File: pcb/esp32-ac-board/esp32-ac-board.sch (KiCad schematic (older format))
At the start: 5 parts, among them Q1 Q_NPN_BCE

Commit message: Fix schematic, redo PCB
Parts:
- added J1, J2: Conn_01x15, Connector_PinHeader_2.54mm:PinHeader_1x15_P2.54mm_Vertical, symbol Connector_Generic:Conn_01x15
- added SW1: SW_Push, Button_Switch_THT:SW_PUSH-12mm, symbol Switch:SW_Push
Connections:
- net labels added: 1, 13, 15, 16, 17, 18, 19, 2, 21, 22, 23, 25, 27, 3, 32, 33, 34, 35, 36, 39, 4, 5, BTN, EN, SEND, TEMP, VCC
- net labels removed: VIN
- wire segments 42 -> 54
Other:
- moved on the sheet: DHT_22, R1

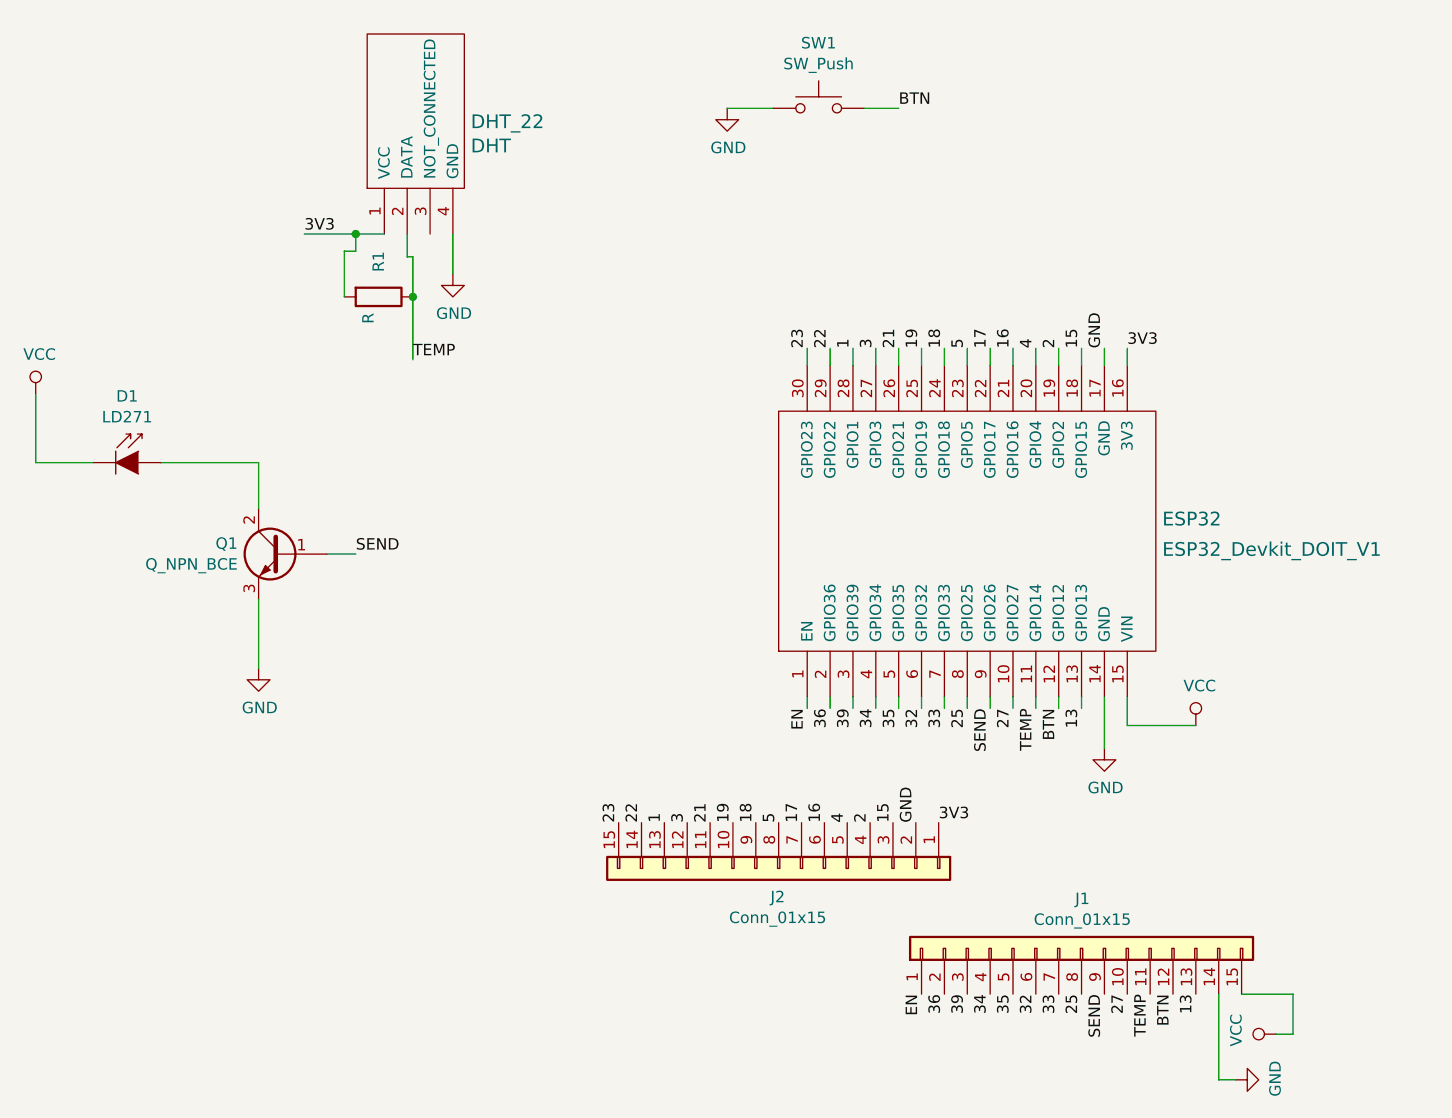
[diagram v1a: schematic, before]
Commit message: Use 5V signal like in https://hackaday.com/2016/11/17/creating-a-pcb-in-everything-kicad-part-1/
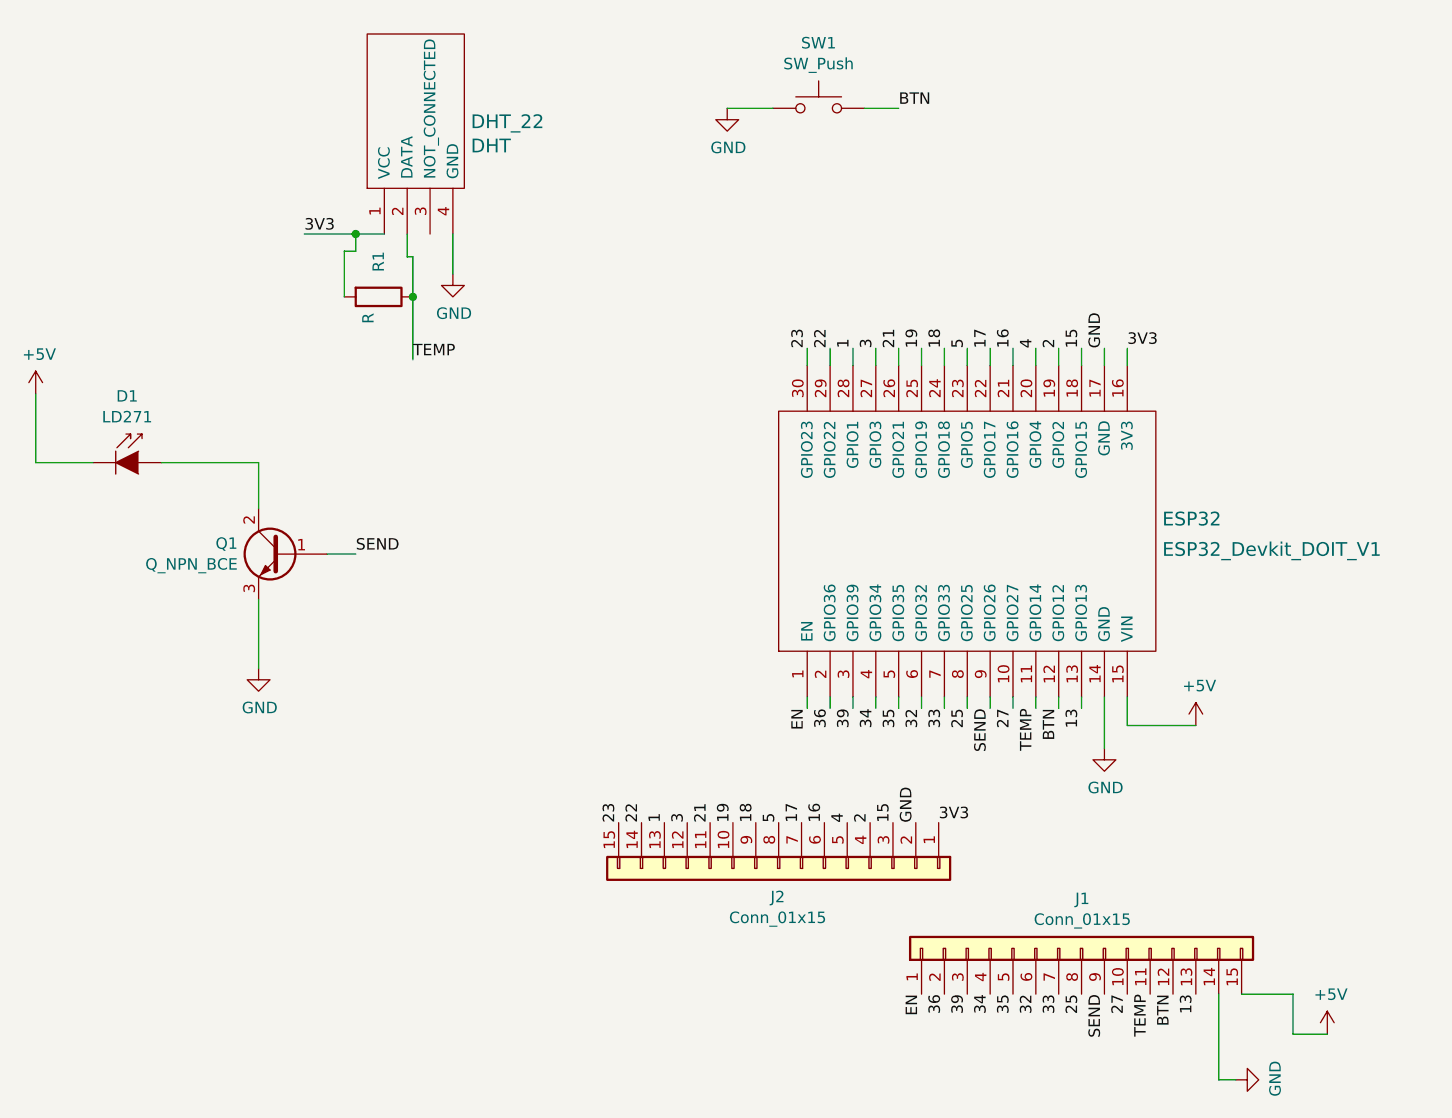
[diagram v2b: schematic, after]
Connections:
- net VCC renamed +5V
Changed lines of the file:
@@
 Wire Wire Line
 	7075 2850 7075 2675
-$Comp
-L power:VCC #PWR01
-U 1 1 5CFF060E
-P 5250 3375
-F 0 "#PWR01" H 5250 3225 50  0001 C CNN
-F 1 "VCC" H 5267 3548 50  0000 C CNN
-F 2 "" H 5250 3375 50  0001 C CNN
-F 3 "" H 5250 3375 50  0001 C CNN
-	1    5250 3375
-	1    0    0    -1
-$EndComp
 Wire Wire Line
 	5250 3675 5500 3675
 Wire Wire Line
 	5250 3375 5250 3675
-$Comp
-L power:VCC #PWR05
-U 1 1 5CFF29F8
-P 10325 4825
-F 0 "#PWR05" H 10325 4675 50  0001 C CNN
-F 1 "VCC" H 10342 4998 50  0000 C CNN
-F 2 "" H 10325 4825 50  0001 C CNN
-F 3 "" H 10325 4825 50  0001 C CNN
-	1    10325 4825
-	1    0    0    -1
-$EndComp
 Wire Wire Line
 	10325 4825 10025 4825
@@
 Wire Wire Line
 	10500 6375 10425 6375
-$Comp
-L power:VCC #PWR0103
-U 1 1 5D01AC3E
-P 10675 6175
-F 0 "#PWR0103" H 10675 6025 50  0001 C CNN
-F 1 "VCC" H 10692 6348 50  0000 C CNN
-F 2 "" H 10675 6175 50  0001 C CNN
-F 3 "" H 10675 6175 50  0001 C CNN
-	1    10675 6175
-	0    -1   -1   0
-$EndComp
-Wire Wire Line
-	10675 6175 10750 6175
+Wire Wire Line
+	10900 6175 10750 6175
 Wire Wire Line
 	10750 6175 10750 6000
@@
 Wire Wire Line
 	8875 2125 9025 2125
+$Comp
+L power:+5V #PWR?
+U 1 1 5CFF5954
+P 5250 3375
+F 0 "#PWR?" H 5250 3225 50  0001 C CNN
+F 1 "+5V" H 5265 3548 50  0000 C CNN
+F 2 "" H 5250 3375 50  0001 C CNN
+F 3 "" H 5250 3375 50  0001 C CNN
+	1    5250 3375
+	1    0    0    -1
+$EndComp
+$Comp
+L power:+5V #PWR?
+U 1 1 5CFF6215
+P 10325 4825
+F 0 "#PWR?" H 10325 4675 50  0001 C CNN
+F 1 "+5V" H 10340 4998 50  0000 C CNN
+F 2 "" H 10325 4825 50  0001 C CNN
+F 3 "" H 10325 4825 50  0001 C CNN
+	1    10325 4825
+	1    0    0    -1
+$EndComp
+$Comp
+L power:+5V #PWR?
+U 1 1 5CFF718F
+P 10900 6175
+F 0 "#PWR?" H 10900 6025 50  0001 C CNN
+F 1 "+5V" H 10915 6348 50  0000 C CNN
+F 2 "" H 10900 6175 50  0001 C CNN
+F 3 "" H 10900 6175 50  0001 C CNN
+	1    10900 6175
+	1    0    0    -1
+$EndComp
 $EndSCHEMATC

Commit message: Add traces
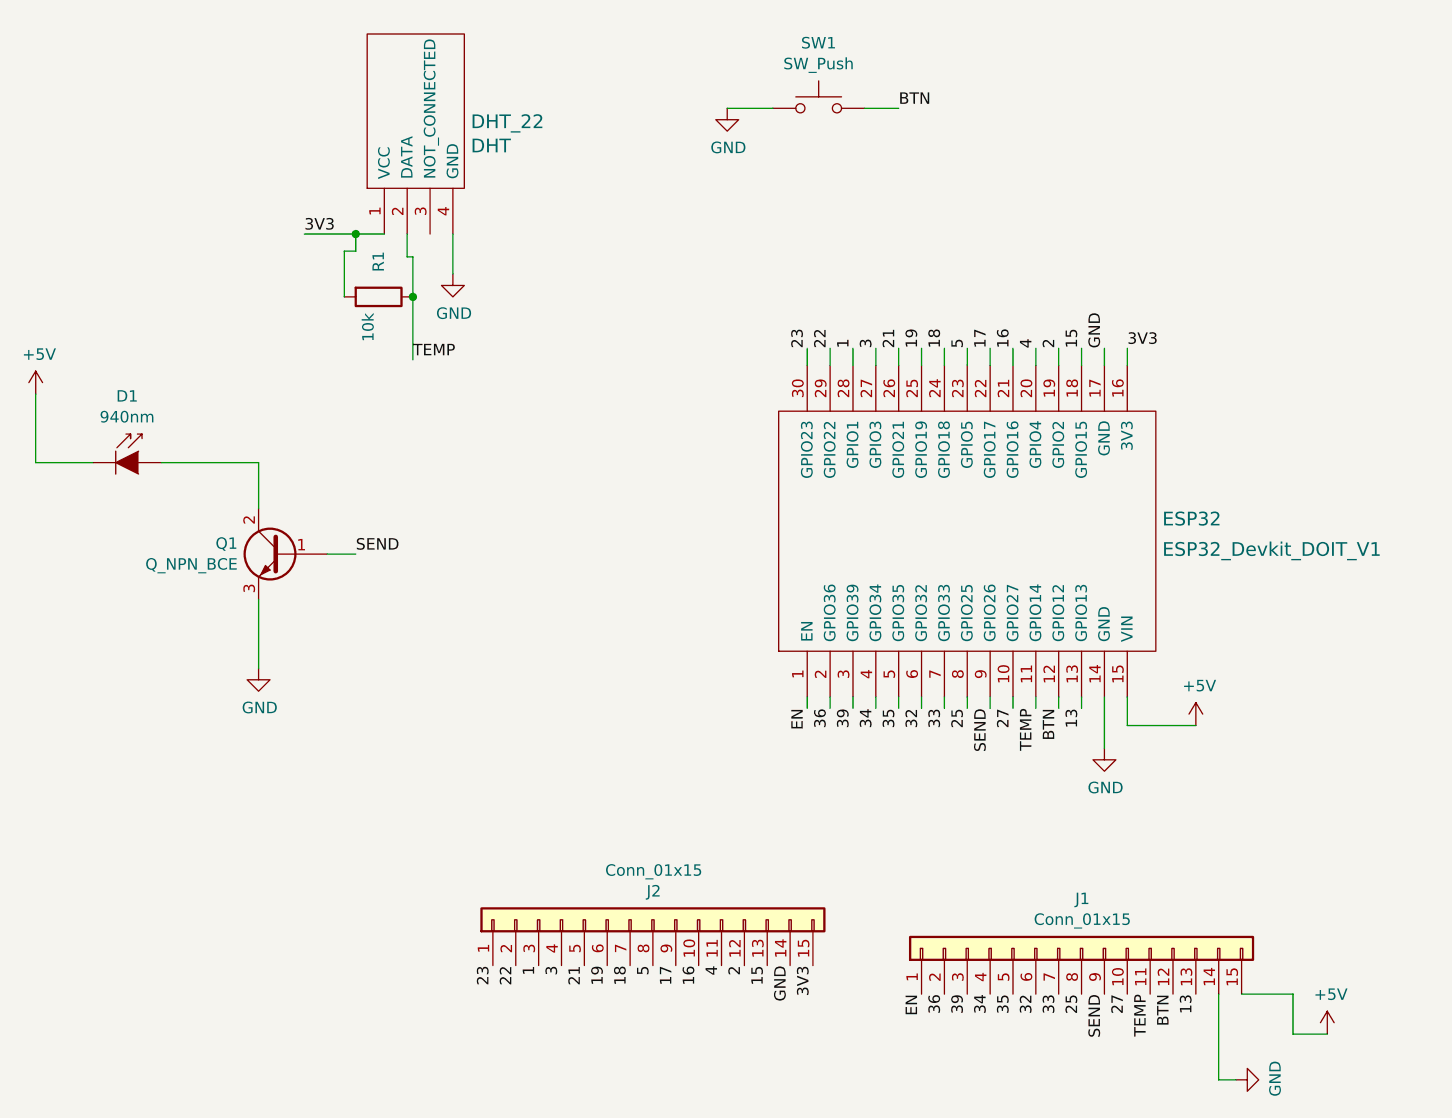
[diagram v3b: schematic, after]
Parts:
- D1: value LD271 -> 940nm
- R1: value R -> 10k
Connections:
- net 1: now also J2.3 (Pin_3); no longer J2.13 (Pin_13)
- net 15: now also J2.13 (Pin_13); no longer J2.3 (Pin_3)
- net 16: now also J2.10 (Pin_10); no longer J2.6 (Pin_6)
- net 17: now also J2.9 (Pin_9); no longer J2.7 (Pin_7)
- net 18: now also J2.7 (Pin_7); no longer J2.9 (Pin_9)
- net 19: now also J2.6 (Pin_6); no longer J2.10 (Pin_10)
- net 2: now also J2.12 (Pin_12); no longer J2.4 (Pin_4)
- net 21: now also J2.5 (Pin_5); no longer J2.11 (Pin_11)
- net 22: now also J2.2 (Pin_2); no longer J2.14 (Pin_14)
- net 23: now also J2.1 (Pin_1); no longer J2.15 (Pin_15)
- net 3: now also J2.4 (Pin_4); no longer J2.12 (Pin_12)
- net 3V3: now also J2.15 (Pin_15); no longer J2.1 (Pin_1)
- net 4: now also J2.11 (Pin_11); no longer J2.5 (Pin_5)
- net GND: now also J2.14 (Pin_14); no longer J2.2 (Pin_2)
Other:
- moved on the sheet: J2
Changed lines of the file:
@@
 P 5700 3675
 F 0 "D1" H 5650 3965 50  0000 C CNN
-F 1 "LD271" H 5650 3874 50  0000 C CNN
+F 1 "940nm" H 5650 3874 50  0000 C CNN
 F 2 "LED_THT:LED_D5.0mm_IRGrey" H 5700 3850 50  0001 C CNN
 F 3 "http://www.alliedelec.com/m/d/40788c34903a719969df15f1fbea1056.pdf" H 5650 3675 50  0001 C CNN
@@
 P 6750 2950
 F 0 "R1" H 6550 2950 50  0000 L CNN
-F 1 "R" H 6820 2905 50  0000 L CNN
+F 1 "10k" H 6820 2905 50  0000 L CNN
 F 2 "Resistor_THT:R_Axial_DIN0204_L3.6mm_D1.6mm_P5.08mm_Horizontal" V 6680 2950 50  0001 C CNN
 F 3 "~" H 6750 2950 50  0001 C CNN
@@
 L Connector_Generic:Conn_01x15 J2
 U 1 1 5D00F2B8
-P 8500 5450
-F 0 "J2" V 8625 5446 50  0000 C CNN
-F 1 "Conn_01x15" V 8716 5446 50  0000 C CNN
-F 2 "Connector_PinHeader_2.54mm:PinHeader_1x15_P2.54mm_Vertical" H 8500 5450 50  0001 C CNN
-F 3 "~" H 8500 5450 50  0001 C CNN
-	1    8500 5450
-	0    1    1    0
+P 7950 5675
+F 0 "J2" V 8075 5671 50  0000 C CNN
+F 1 "Conn_01x15" V 8166 5671 50  0000 C CNN
+F 2 "Connector_PinHeader_2.54mm:PinHeader_1x15_P2.54mm_Vertical" H 7950 5675 50  0001 C CNN
+F 3 "~" H 7950 5675 50  0001 C CNN
+	1    7950 5675
+	0    -1   -1   0
 $EndComp
 Text Label 8625 4750 3    50   ~ 0
@@
 Wire Wire Line
 	6225 4275 6225 4575
-Text Label 9200 5250 0    50   ~ 0
+Text Label 8650 5875 3    50   ~ 0
 3V3
-Text Label 9100 5250 1    50   ~ 0
+Text Label 8550 5875 3    50   ~ 0
 GND
-Text Label 9000 5250 1    50   ~ 0
+Text Label 8450 5875 3    50   ~ 0
 15
-Text Label 8900 5250 1    50   ~ 0
+Text Label 8350 5875 3    50   ~ 0
 2
 Text Label 9925 3175 1    50   ~ 0
@@
 Text Label 8625 3175 1    50   ~ 0
 23
-Text Label 8800 5250 1    50   ~ 0
+Text Label 8250 5875 3    50   ~ 0
 4
-Text Label 8700 5250 1    50   ~ 0
+Text Label 8150 5875 3    50   ~ 0
 16
-Text Label 8600 5250 1    50   ~ 0
+Text Label 8050 5875 3    50   ~ 0
 17
-Text Label 8500 5250 1    50   ~ 0
+Text Label 7950 5875 3    50   ~ 0
 5
-Text Label 8400 5250 1    50   ~ 0
+Text Label 7850 5875 3    50   ~ 0
 18
-Text Label 8300 5250 1    50   ~ 0
+Text Label 7750 5875 3    50   ~ 0
 19
-Text Label 8200 5250 1    50   ~ 0
+Text Label 7650 5875 3    50   ~ 0
 21
-Text Label 8100 5250 1    50   ~ 0
+Text Label 7550 5875 3    50   ~ 0
 3
-Text Label 8000 5250 1    50   ~ 0
+Text Label 7450 5875 3    50   ~ 0
 1
-Text Label 7900 5250 1    50   ~ 0
+Text Label 7350 5875 3    50   ~ 0
 22
-Text Label 7800 5250 1    50   ~ 0
+Text Label 7250 5875 3    50   ~ 0
 23
 $Comp
@@
 	8875 2125 9025 2125
 $Comp
-L power:+5V #PWR?
+L power:+5V #PWR0103
 U 1 1 5CFF5954
 P 5250 3375
-F 0 "#PWR?" H 5250 3225 50  0001 C CNN
+F 0 "#PWR0103" H 5250 3225 50  0001 C CNN
 F 1 "+5V" H 5265 3548 50  0000 C CNN
 F 2 "" H 5250 3375 50  0001 C CNN
@@
 $EndComp
 $Comp
-L power:+5V #PWR?
+L power:+5V #PWR0104
 U 1 1 5CFF6215
 P 10325 4825
-F 0 "#PWR?" H 10325 4675 50  0001 C CNN
+F 0 "#PWR0104" H 10325 4675 50  0001 C CNN
 F 1 "+5V" H 10340 4998 50  0000 C CNN
 F 2 "" H 10325 4825 50  0001 C CNN
@@
 $EndComp
 $Comp
-L power:+5V #PWR?
+L power:+5V #PWR0105
 U 1 1 5CFF718F
 P 10900 6175
-F 0 "#PWR?" H 10900 6025 50  0001 C CNN
+F 0 "#PWR0105" H 10900 6025 50  0001 C CNN
 F 1 "+5V" H 10915 6348 50  0000 C CNN
 F 2 "" H 10900 6175 50  0001 C CNN

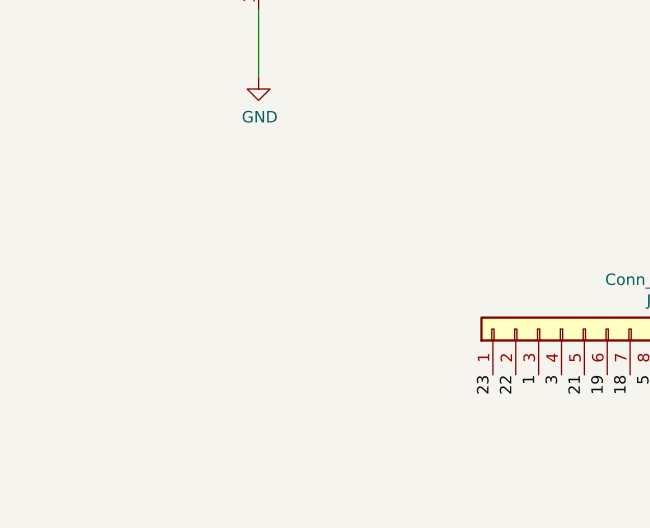
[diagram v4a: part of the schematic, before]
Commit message: add screw terminal for power
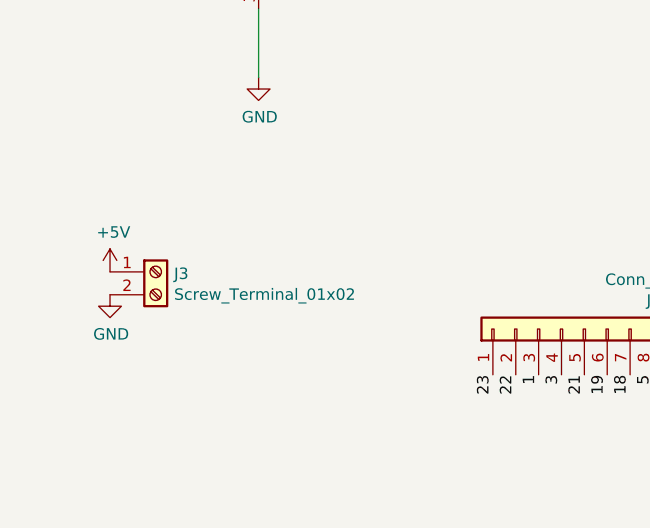
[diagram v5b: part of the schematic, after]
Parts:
- added J3: Screw_Terminal_01x02, TerminalBlock:TerminalBlock_bornier-2_P5.08mm, symbol Connector:Screw_Terminal_01x02
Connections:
- net +5V: now also J3.1 (Pin_1)
- net GND: now also J3.2 (Pin_2)
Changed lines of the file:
@@
 Text Label 9925 3175 1    50   ~ 0
 GND
+$Comp
+L Connector:Screw_Terminal_01x02 J3
+U 1 1 5D014690
+P 5775 5425
+F 0 "J3" H 5855 5417 50  0000 L CNN
+F 1 "Screw_Terminal_01x02" H 5855 5326 50  0000 L CNN
+F 2 "TerminalBlock:TerminalBlock_bornier-2_P5.08mm" H 5775 5425 50  0001 C CNN
+F 3 "~" H 5775 5425 50  0001 C CNN
+	1    5775 5425
+	1    0    0    -1
+$EndComp
+$Comp
+L power:+5V #PWR0106
+U 1 1 5D016026
+P 5575 5425
+F 0 "#PWR0106" H 5575 5275 50  0001 C CNN
+F 1 "+5V" H 5590 5598 50  0000 C CNN
+F 2 "" H 5575 5425 50  0001 C CNN
+F 3 "" H 5575 5425 50  0001 C CNN
+	1    5575 5425
+	1    0    0    -1
+$EndComp
+$Comp
+L power:GND #PWR0107
+U 1 1 5D016A88
+P 5575 5525
+F 0 "#PWR0107" H 5575 5275 50  0001 C CNN
+F 1 "GND" H 5580 5352 50  0000 C CNN
+F 2 "" H 5575 5525 50  0001 C CNN
+F 3 "" H 5575 5525 50  0001 C CNN
+	1    5575 5525
+	1    0    0    -1
+$EndComp
 $EndSCHEMATC

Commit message: attempt to rotate diode
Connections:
- net +5V: now also D1.2 (A); no longer D1.1 (K)
- net at Q1.2 (C): now also D1.1 (K); no longer D1.2 (A)
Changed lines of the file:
@@
 L LED:LD271 D1
 U 1 1 5CFE8B8D
-P 5700 3675
-F 0 "D1" H 5650 3965 50  0000 C CNN
-F 1 "940nm" H 5650 3874 50  0000 C CNN
-F 2 "LED_THT:LED_D5.0mm_IRGrey" H 5700 3850 50  0001 C CNN
-F 3 "http://www.alliedelec.com/m/d/40788c34903a719969df15f1fbea1056.pdf" H 5650 3675 50  0001 C CNN
-	1    5700 3675
-	1    0    0    -1
+P 5600 3675
+F 0 "D1" H 5550 3965 50  0000 C CNN
+F 1 "940nm" H 5550 3874 50  0000 C CNN
+F 2 "LED_THT:LED_D5.0mm_IRGrey" H 5600 3850 50  0001 C CNN
+F 3 "http://www.alliedelec.com/m/d/40788c34903a719969df15f1fbea1056.pdf" H 5550 3675 50  0001 C CNN
+	1    5600 3675
+	-1   0    0    -1
 $EndComp
 Wire Wire Line
@@
 Wire Wire Line
 	6225 3875 6225 3675
-Wire Wire Line
-	6225 3675 5800 3675
 Wire Wire Line
 	6875 2775 6875 2675
@@
 	1    0    0    -1
 $EndComp
+Wire Wire Line
+	5800 3675 6225 3675
 $EndSCHEMATC

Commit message: fix button holes
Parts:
- SW1: footprint Button_Switch_THT:SW_PUSH-12mm -> Button_Switch_THT:SW_PUSH-12mm_Wuerth-430476085716
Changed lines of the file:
@@
 EESchema Schematic File Version 4
 LIBS:esp32-ac-board-cache
-EELAYER 29 0
+EELAYER 26 0
 EELAYER END
 $Descr A4 11693 8268
@@
 F 0 "SW1" H 8675 2410 50  0000 C CNN
 F 1 "SW_Push" H 8675 2319 50  0000 C CNN
-F 2 "Button_Switch_THT:SW_PUSH-12mm" H 8675 2325 50  0001 C CNN
+F 2 "Button_Switch_THT:SW_PUSH-12mm_Wuerth-430476085716" H 8675 2325 50  0001 C CNN
 F 3 "~" H 8675 2325 50  0001 C CNN
 	1    8675 2125
